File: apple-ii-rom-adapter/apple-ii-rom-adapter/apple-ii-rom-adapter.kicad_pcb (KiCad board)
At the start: 2 copper layers, 11 parts, among them J1 ROMSEL, J2 9316 insert, J3 74LS138 insert, U1 28C256, U2 74LS00, U3 74LS138

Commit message: Incremental update! Maybe this'll work? :-)
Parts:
- C1, C2, C3: footprint Capacitor_THT:CP_Radial_D6.3mm_P2.50mm -> Capacitor_THT:C_Disc_D5.0mm_W2.5mm_P5.00mm
- moved C3 96.5 mm to (43.7, 16.0), turned to 270 degrees
- moved C2 91.3 mm to (43.7, 28.2), turned to 90 degrees
- moved U2 89.8 mm to (49.0, 16.5)
- moved U3 85.6 mm to (40.4, 20.1), turned to 270 degrees
- moved J1 78.2 mm to (54.4, 37.3)
- moved J3 77.8 mm to (40.4, 17.8), turned to 270 degrees
- moved R1 74.5 mm to (60.7, 32.3), turned to 90 degrees
- moved C1 60.9 mm to (54.1, 52.8), turned to 90 degrees
- moved R2 53.0 mm to (58.9, 52.6), turned to 90 degrees
- moved J2 50.5 mm to (45.5, 31.8), turned to 270 degrees
- moved U1 33.5 mm to (50.5, 37.1), turned to 270 degrees
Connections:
- R2 pad 1: Net-(R2-Pad1) -> VCC
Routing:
- net VCC: track 0.00 -> 63.1 mm
- net A_PD: track 0.00 -> 56.0 mm, vias 0 -> 1
- net N_OE: track 0.00 -> 52.1 mm
- net N_CS: track 0.00 -> 44.5 mm
- net A13: track 0.00 -> 42.9 mm, vias 0 -> 2
- net A11: track 0.00 -> 35.6 mm
- net Net-(R1-Pad1): track 0.00 -> 31.9 mm
- net A12: track 0.00 -> 28.7 mm
- net A_SEL_0: track 0.00 -> 26.0 mm, vias 0 -> 1
- net A_SEL_1: track 0.00 -> 22.9 mm, vias 0 -> 1
- net A8: track 0.00 -> 21.6 mm
- net Net-(U2-Pad3): track 0.00 -> 13.6 mm
- net Net-(U2-Pad10): track 0.00 -> 9.27 mm
- net GND: track 0.00 -> 7.62 mm
- net A14: track 0.00 -> 6.31 mm
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- added copper zone on B.Cu, net GND
- added copper zone on F.Cu, net GND
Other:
- board outline added: 51.6 x 43.9 mm
- board text added: "28C256 to Apple-ii Rev0 Proto 0.1 Adrian Chadd <adrian@freebsd.org> 11/June/2021"

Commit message: whoops, missed a connection!
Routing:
- net A_SEL_0: track 26.0 -> 28.3 mm

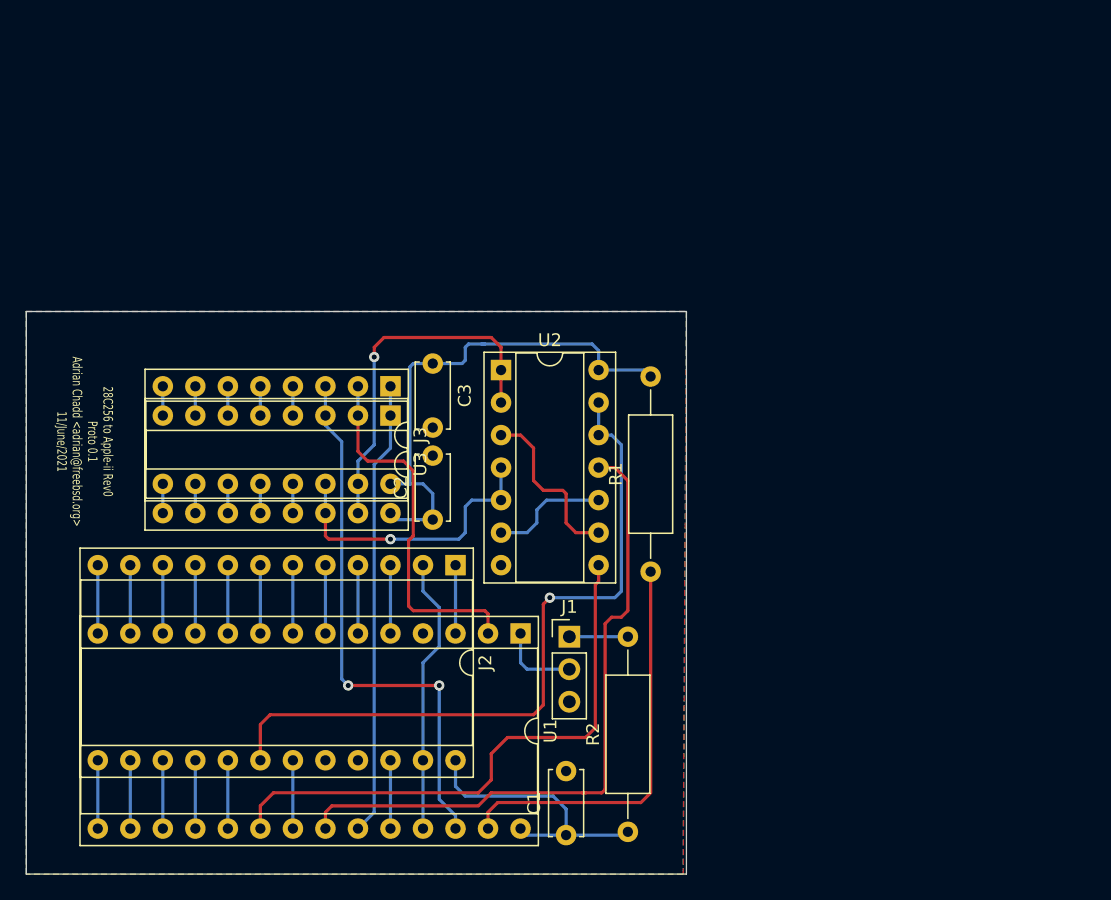
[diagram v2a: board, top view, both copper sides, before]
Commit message: Updates to actually make this work!
It didn't work with this plugged in, ROM or not populated.

* Wow, I screwed up the address line naming, whoops, that removes a short
  across two address lines so now the apple-ii will boot with this plugged
  in w/ the 74LS138 populated but ROMs in the normal ROM slots.

* Wow, I fucked up the logic.  The logic I chose plainly wouldn't work.
  Replace it with a pair of NAND gates and a NOR gate to implement the
  correct /CS logic.  This now boots to integer basic.

Tested:

* integer basic image with original non autostart monitor - E000G jumps
  to integer BASIC fine.

* integer basic image with language card installed - the autostart
  monitor does indeed jump to integer basic AND this demonstrates the
  inhibit line logic works fine.

Aiee, etc.
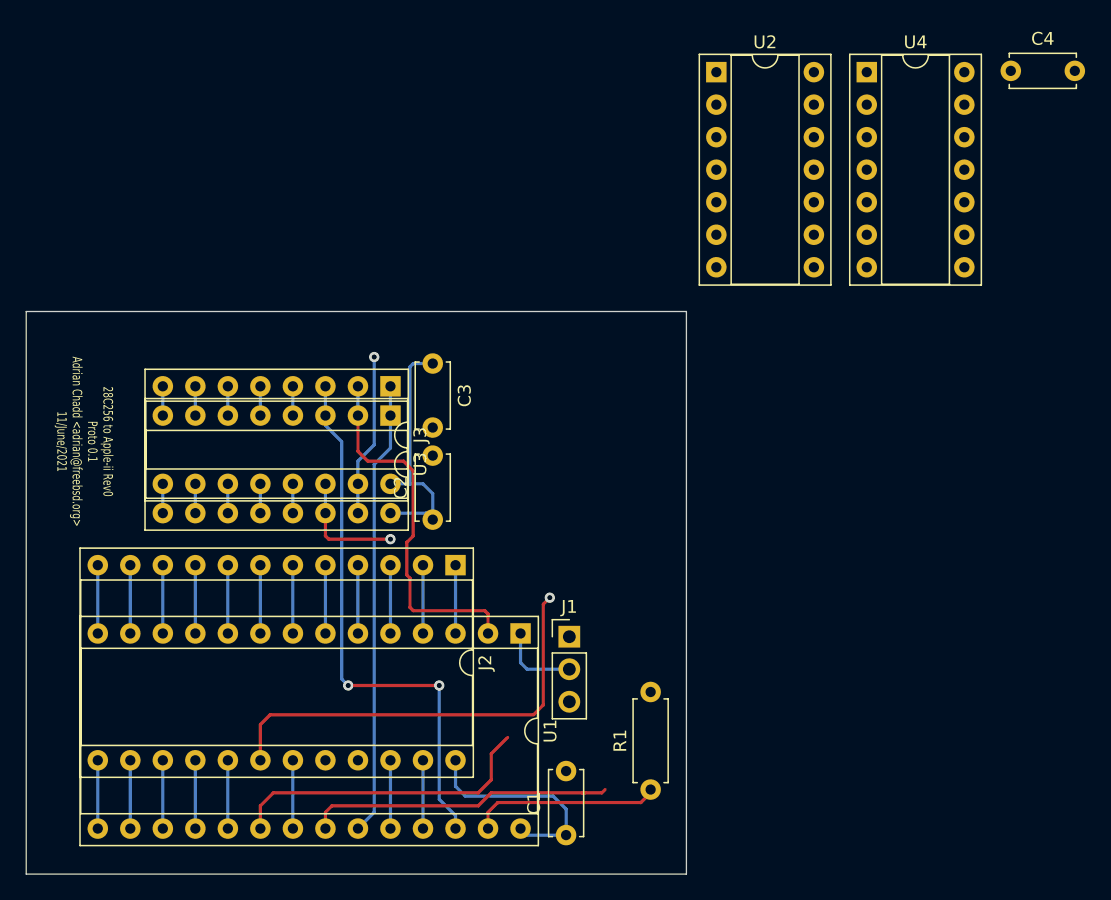
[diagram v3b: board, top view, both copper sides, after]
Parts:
- removed R2: 1K, Resistor_THT:R_Axial_DIN0309_L9.0mm_D3.2mm_P15.24mm_Horizontal
- added C4: 0.1uF, Capacitor_THT:C_Disc_D5.0mm_W2.5mm_P5.00mm, F.Cu at (88.8, -6.86)
- added U4: 74LS02, Package_DIP:DIP-14_W7.62mm_Socket, F.Cu at (77.6, -6.76)
- R1: footprint Resistor_THT:R_Axial_DIN0309_L9.0mm_D3.2mm_P15.24mm_Horizontal -> Resistor_THT:R_Axial_DIN0207_L6.3mm_D2.5mm_P7.62mm_Horizontal
- U2: value 74LS00 -> 74LS20
- moved U2 28.7 mm to (65.8, -6.76)
- moved R1 17.0 mm to (60.7, 49.3)
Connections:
- J1 pad 1: Net-(J1-Pad1) -> SOFT_5
- J2 pad 2: A8 -> A6
- R1 pad 1: Net-(R1-Pad1) -> SOFT_5
- U1 pad 27: Net-(R1-Pad1) -> SOFT_5
- U2 pad 1: A_SEL_0 -> SOFT_5
- U2 pad 10: Net-(U2-Pad10) -> A_SEL_5
- U2 pad 11: N_OE -> (no net)
- U2 pad 12: A_PD -> A_SEL_6
- U2 pad 13: A_PD -> A_SEL_7
- U2 pad 2: A_SEL_0 -> SOFT_5
- U2 pad 3: Net-(U2-Pad3) -> (no net)
- U2 pad 4: A_SEL_1 -> A_SEL_2
- U2 pad 5: A_SEL_1 -> A_SEL_3
- U2 pad 6: Net-(U2-Pad10) -> Net-(U2-Pad6)
- U2 pad 8: N_CS -> Net-(U2-Pad8)
- U2 pad 9: Net-(U2-Pad3) -> A_SEL_4
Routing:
- net Net-(R1-Pad1): track 31.9 -> 0.00 mm
- net N_OE: track 52.1 -> 24.1 mm
- net VCC: track 63.1 -> 38.5 mm
- net A_PD: track 56.0 -> 34.1 mm
- net N_CS: track 44.5 -> 24.5 mm
- net A8: track 21.6 -> 5.33 mm
- net A_SEL_0: track 28.3 -> 12.7 mm
- net SOFT_5: track 0.00 -> 14.6 mm
- net A_SEL_1: track 22.9 -> 9.25 mm
- net Net-(U2-Pad3): track 13.6 -> 0.00 mm
- net Net-(U2-Pad10): track 9.27 -> 0.00 mm
- net A6: track 0.00 -> 5.33 mm
- net Net-(J1-Pad1): track 4.57 -> 0.00 mm
- removed copper zone on B.Cu, net GND
- removed copper zone on F.Cu, net GND

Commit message: Rom adapter update
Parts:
- removed C1: 0.1uF, Capacitor_THT:C_Disc_D5.0mm_W2.5mm_P5.00mm
- moved U4 46.1 mm to (54.4, 33.0)
- moved C4 40.8 mm to (63.5, 25.1), turned to 90 degrees
- moved U2 39.1 mm to (44.7, 26.2), turned to 90 degrees
- moved R1 20.8 mm to (54.4, 29.5), turned to 0 degrees
- moved J1 16.2 mm to (56.6, 53.3), turned to 90 degrees
- moved C2 13.0 mm to (45.0, 15.2), turned to 0 degrees
- moved C3 4.44 mm to (39.4, 15.0), turned to 180 degrees
- moved J2 1.61 mm to (43.9, 32.3)
- moved U3 1.61 mm to (38.9, 20.6)
- moved J3 1.61 mm to (38.9, 18.3)
- moved U1 1.61 mm to (49.0, 37.6)
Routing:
- net SOFT_5: track 14.6 -> 63.1 mm
- net A_SEL_5: track 2.29 -> 40.6 mm
- net A_SEL_4: track 2.29 -> 40.6 mm
- net A_SEL_6: track 2.29 -> 38.3 mm
- net Net-(U2-Pad8): track 0.00 -> 32.6 mm
- net A_SEL_3: track 2.29 -> 32.7 mm
- net A_SEL_7: track 2.29 -> 30.2 mm
- net VCC: track 38.5 -> 66.3 mm, vias 0 -> 2
- net A_SEL_2: track 2.29 -> 26.4 mm
- net Net-(U2-Pad6): track 0.00 -> 19.9 mm
- net N_OE: track 24.1 -> 43.2 mm
- net A14: track 6.31 -> 25.2 mm
- net N_CS: track 24.5 -> 35.6 mm
- net A_SEL_0: track 12.7 -> 2.29 mm, vias 1 -> 0
- net A12: track 28.8 -> 37.3 mm, vias 0 -> 2
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- added copper zone on B.Cu, net GND
- added copper zone on F.Cu, net GND
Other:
- board size 51.6 x 43.9 mm -> 53.6 x 45.2 mm
- board text added: "28C256 to Apple-ii Rev0 Proto 0.2 Adrian Chadd <adrian@freebsd.org> 1/July/2021"
- board text removed: "28C256 to Apple-ii Rev0 Proto 0.1 Adrian Chadd <adrian@freebsd.org> 11/June/2021"
